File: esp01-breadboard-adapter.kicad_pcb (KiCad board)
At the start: 2 copper layers, 15.2 x 17.4 mm, 4 parts, among them P1 CONN_02X04, P2 CONN_01X04, P3 CONN_01X04

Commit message: edited schematic
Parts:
- removed P2, P3: CONN_01X04, Pin_Headers:Pin_Header_Straight_1x04
- moved P1 24.7 mm to (153.7, 106.7), turned to 0 degrees
- moved C1 4.10 mm to (135.9, 110.5), turned to 270 degrees
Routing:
- net GND: track 18.4 -> 0.00 mm, vias 1 -> 0
- net GPIO0: track 16.4 -> 0.00 mm, vias 1 -> 0
- net GPIO2: track 16.1 -> 0.00 mm, vias 1 -> 0
- net VCC: track 15.8 -> 0.00 mm, vias 1 -> 0
- net RXD: track 10.9 -> 0.00 mm, vias 1 -> 0
- net RESET: track 10.8 -> 0.00 mm, vias 1 -> 0
- net CH_PD: track 10.7 -> 0.00 mm, vias 1 -> 0
- net TXD: track 4.50 -> 0.00 mm, vias 1 -> 0
- removed copper zone on B.Cu, net GND
- removed copper zone on F.Cu, net VCC
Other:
- board outline removed
- board text removed: "CH_PD"
- board text removed: "GND"
- board text removed: "GPIO0"
- board text removed: "GPIO2"
- board text removed: "RESET"
- board text removed: "RXD"
- board text removed: "TXD"
- board text removed: "VCC"
- board text removed: "github.com/fu0x11"

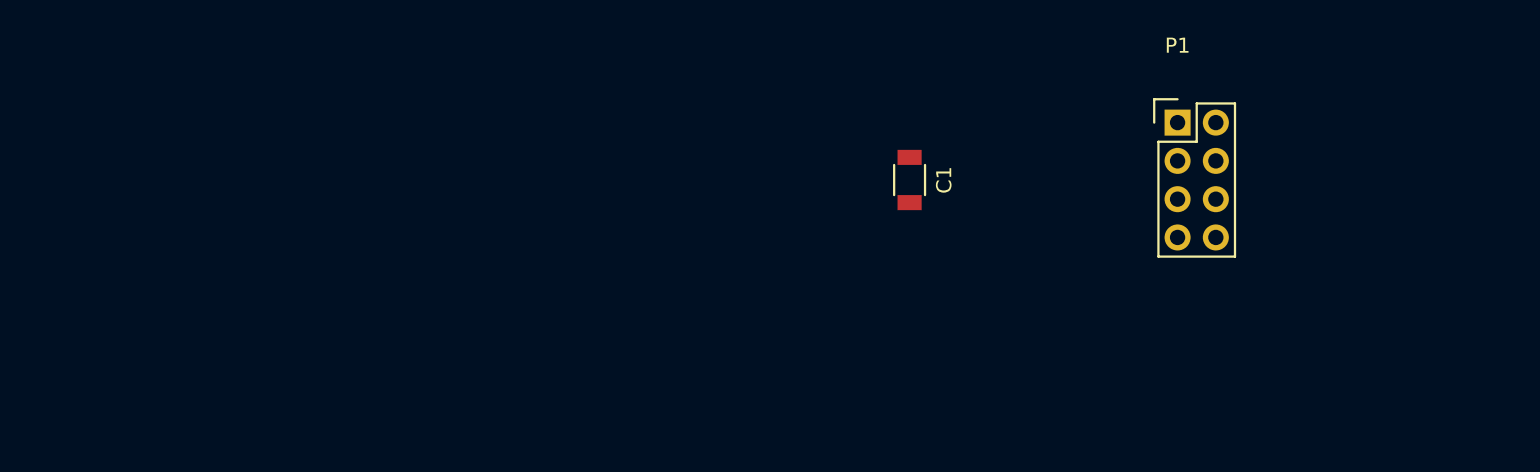
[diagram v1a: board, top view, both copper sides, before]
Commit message: new pcb layout, fix connection
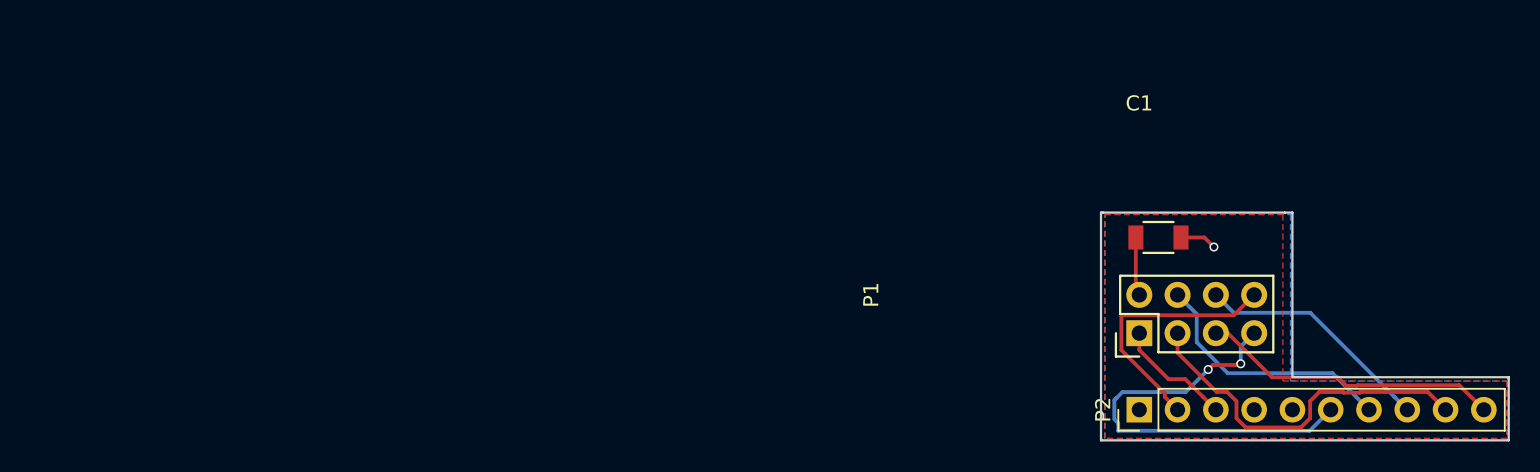
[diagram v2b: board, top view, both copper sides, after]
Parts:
- added P2: CONN_01X10, Pin_Headers:Pin_Header_Straight_1x10_Pitch2.54mm, F.Cu at (151.1, 125.7)
- moved C1 16.9 mm to (152.4, 114.3), turned to 0 degrees
- moved P1 14.2 mm to (151.1, 120.7), turned to 90 degrees
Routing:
- net GND: track 0.00 -> 31.3 mm, vias 0 -> 3
- net GPIO0: track 0.00 -> 24.0 mm
- net GPIO2: track 0.00 -> 19.9 mm
- net TXD: track 0.00 -> 17.1 mm
- net RESET: track 0.00 -> 17.0 mm
- net CH_PD: track 0.00 -> 15.9 mm
- net RXD: track 0.00 -> 7.84 mm
- net VCC: track 0.00 -> 3.91 mm
- added copper zone on B.Cu, net GND
- added copper zone on F.Cu, net VCC
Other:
- board outline added: 27.1 x 15.1 mm

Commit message: pcb complete
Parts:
- moved P2 68.4 mm to (83.0, 120.8)
- moved P1 68.3 mm to (83.0, 117.0)
- moved C1 58.6 mm to (93.8, 115.1), turned to 270 degrees
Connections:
- P2 pad 10: GPIO2 -> CH_PD
- P2 pad 8: CH_PD -> GPIO0
- P2 pad 9: GPIO0 -> GPIO2
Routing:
- net GND: track 31.3 -> 3.43 mm, vias 3 -> 0
- net GPIO0: track 24.0 -> 16.8 mm
- net CH_PD: track 15.9 -> 22.0 mm
- net VCC: track 3.91 -> 0.00 mm
- net GPIO2: track 19.9 -> 17.5 mm
- net TXD: track 17.1 -> 14.8 mm
- net RXD: track 7.84 -> 7.29 mm
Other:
- board size 27.1 x 15.1 mm -> 26.7 x 10.2 mm
- board text added: "github.com/fu0x11"

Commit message: added front silkscreen
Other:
- board text added: "CH_PD"
- board text added: "GND"
- board text added: "GPIO0"
- board text added: "GPIO2"
- board text added: "RESET"
- board text added: "RXD"
- board text added: "TXD"
- board text added: "VCC"
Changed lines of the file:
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@@
     (area 80.569999 112.319999 107.390001 122.630001)
     (thickness 1.6)
-    (drawings 7)
+    (drawings 15)
     (tracks 39)
     (zones 0)
@@
     (34 B.Paste user)
     (35 F.Paste user)
-    (36 B.SilkS user)
-    (37 F.SilkS user)
+    (36 B.SilkS user hide)
+    (37 F.SilkS user hide)
     (38 B.Mask user)
     (39 F.Mask user)
@@
       (effects (font (size 1 1) (thickness 0.15)))
     )
-    (fp_text value CONN_02X04 (at 5.8674 -0.4064 180) (layer F.Fab)
+    (fp_text value CONN_02X04 (at 5.8674 -0.4064 180) (layer F.Fab) hide
       (effects (font (size 1 1) (thickness 0.15)))
     )
@@
     (tags "capacitor 1206")
     (attr smd)
-    (fp_text reference C1 (at -2.794 -5.4864 360) (layer F.SilkS)
-      (effects (font (size 1 1) (thickness 0.15)))
-    )
-    (fp_text value 100u (at -1.7145 -6.1849 360) (layer F.Fab)
+    (fp_text reference C1 (at -2.794 -5.4864 360) (layer F.SilkS) hide
+      (effects (font (size 1 1) (thickness 0.15)))
+    )
+    (fp_text value 100u (at -1.7145 -6.1849 360) (layer F.Fab) hide
       (effects (font (size 1 1) (thickness 0.15)))
     )
@@
     (descr "Through hole straight pin header, 1x10, 2.54mm pitch, single row")
     (tags "Through hole pin header THT 1x10 2.54mm single row")
-    (fp_text reference P2 (at -3.0734 0.2286 180) (layer F.SilkS)
-      (effects (font (size 1 1) (thickness 0.15)))
-    )
-    (fp_text value CONN_01X10 (at -4.3434 4.0386 180) (layer F.Fab)
+    (fp_text reference P2 (at -3.0734 0.2286 180) (layer F.SilkS) hide
+      (effects (font (size 1 1) (thickness 0.15)))
+    )
+    (fp_text value CONN_01X10 (at -4.3434 4.0386 180) (layer F.Fab) hide
       (effects (font (size 1 1) (thickness 0.15)))
     )
@@
     )
   )
-  (gr_text github.com/fu0x11 (at 104.775 118.745) (layer B.SilkS)
-    (effects (font (size 0.3 0.3) (thickness 0.075)) (justify mirror))
+  (gr_text CH_PD (at 106.045 118.745) (layer F.SilkS)
+    (effects (font (size 0.5 0.5) (thickness 0.125)))
+  )
+  (gr_text GPIO2 (at 103.505 118.745) (layer F.SilkS)
+    (effects (font (size 0.5 0.5) (thickness 0.125)))
+  )
+  (gr_text GPIO0 (at 100.965 118.745) (layer F.SilkS)
+    (effects (font (size 0.5 0.5) (thickness 0.125)))
+  )
+  (gr_text RESET (at 98.425 118.745) (layer F.SilkS)
+    (effects (font (size 0.5 0.5) (thickness 0.125)))
+  )
+  (gr_text GND (at 95.885 118.745) (layer F.SilkS)
+    (effects (font (size 0.5 0.5) (thickness 0.125)))
+  )
+  (gr_text VCC (at 90.805 118.745) (layer F.SilkS)
+    (effects (font (size 0.5 0.5) (thickness 0.125)))
+  )
+  (gr_text RXD (at 88.265 118.745) (layer F.SilkS)
+    (effects (font (size 0.5 0.5) (thickness 0.125)))
+  )
+  (gr_text TXD (at 85.725 118.745) (layer F.SilkS)
+    (effects (font (size 0.5 0.5) (thickness 0.125)))
+  )
+  (gr_text github.com/fu0x11 (at 102.87 118.745) (layer B.SilkS)
+    (effects (font (size 0.6 0.6) (thickness 0.075)) (justify mirror))
   )
   (gr_line (start 80.645 122.555) (end 80.645 112.395) (angle 90) (layer Edge.Cuts) (width 0.15))

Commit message: updated img and silkscreen
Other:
- board text added: "github.com/fu0x11/esp8266-breadboard-adapter"
- board text removed: "github.com/fu0x11"
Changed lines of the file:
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@@
     (effects (font (size 0.5 0.5) (thickness 0.125)))
   )
-  (gr_text github.com/fu0x11 (at 102.87 118.745) (layer B.SilkS)
-    (effects (font (size 0.6 0.6) (thickness 0.075)) (justify mirror))
+  (gr_text github.com/fu0x11/esp8266-breadboard-adapter (at 99.06 118.745) (layer B.SilkS)
+    (effects (font (size 0.4 0.4) (thickness 0.075)) (justify mirror))
   )
   (gr_line (start 80.645 122.555) (end 80.645 112.395) (angle 90) (layer Edge.Cuts) (width 0.15))
